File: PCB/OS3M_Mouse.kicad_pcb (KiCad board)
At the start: 4 copper layers, 60.8 x 61.3 mm, 47 parts, among them J1 DBG_HDR, J2 USB_C_Receptacle_USB2.0, J3 EXP_HDR, SW1 SW_Push, U1 AP2112K-3.3, U2 LDC1614, U3 STM32F042F6P6, U4 LDC1612, U5 USBLC6-2SC6, X1 ASV-40.000MHz

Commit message: Swapped inner layers to get GND plane close to components, fixed shorted UART
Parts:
- added TP1: TestPoint, TestPoint:TestPoint_Pad_D1.0mm, B.Cu at (149.5, 74.7)
- added TP2: TestPoint, TestPoint:TestPoint_Pad_D1.0mm, B.Cu at (141.8, 74.1)
- added TP3: TestPoint, TestPoint:TestPoint_Pad_D1.0mm, B.Cu at (143.6, 75.1)
- added TP4: TestPoint, TestPoint:TestPoint_Pad_D1.0mm, B.Cu at (141.8, 76.1)
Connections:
- U3 pad 10: unconnected-(U3-Pad10) -> Net-(U3-PA4)
- U3 pad 11: unconnected-(U3-Pad11) -> Net-(U3-PA5)
- U3 pad 12: unconnected-(U3-Pad12) -> Net-(U3-PA6)
- U3 pad 13: unconnected-(U3-Pad13) -> Net-(U3-PA7)
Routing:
- net Net-(U3-PA7): track 0.00 -> 2.40 mm, vias 0 -> 1
- net Net-(U3-PA4): track 0.00 -> 2.04 mm, vias 0 -> 1
- net Net-(U3-PA6): track 0.00 -> 1.95 mm, vias 0 -> 1
- net /UART2_TX: track 39.4 -> 40.6 mm
- net +3.3V: track 90.9 -> 89.8 mm
- net /UART2_RX: track 43.7 -> 44.4 mm, vias 2 -> 3
- net Net-(U3-PA5): track 0.00 -> 0.60 mm, vias 0 -> 1
- net /LDC1614_INTB: track 34.8 -> 34.2 mm
- added copper zone on In2.Cu, net +3.3V
- added copper zone on In1.Cu, net GND
- added copper zone on In2.Cu, net VBUS
- removed copper zone on In1.Cu, net +3.3V
- removed copper zone on In2.Cu, net GND
- removed copper zone on In1.Cu, net VBUS

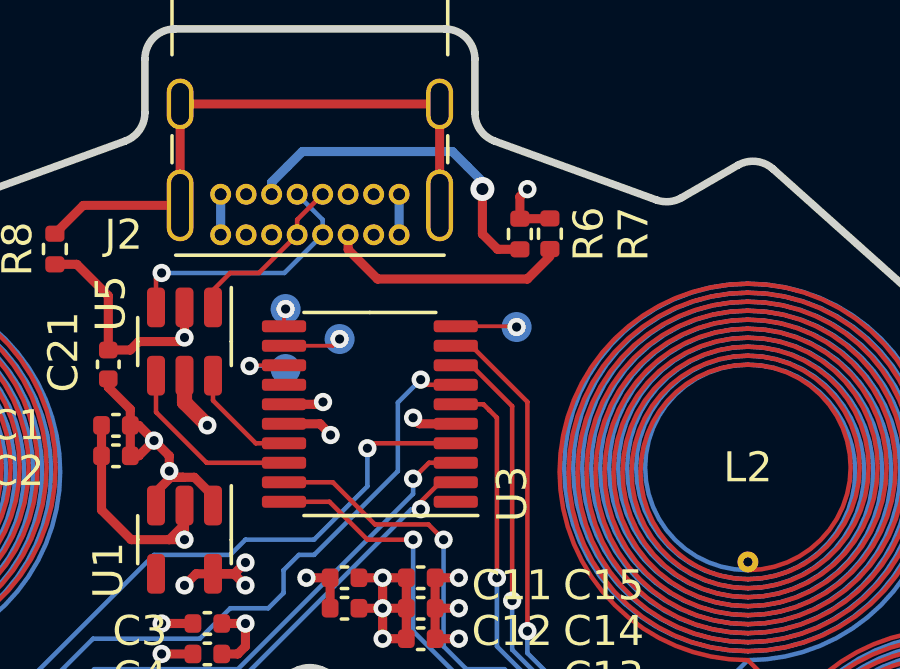
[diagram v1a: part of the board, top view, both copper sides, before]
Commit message: Moved test points
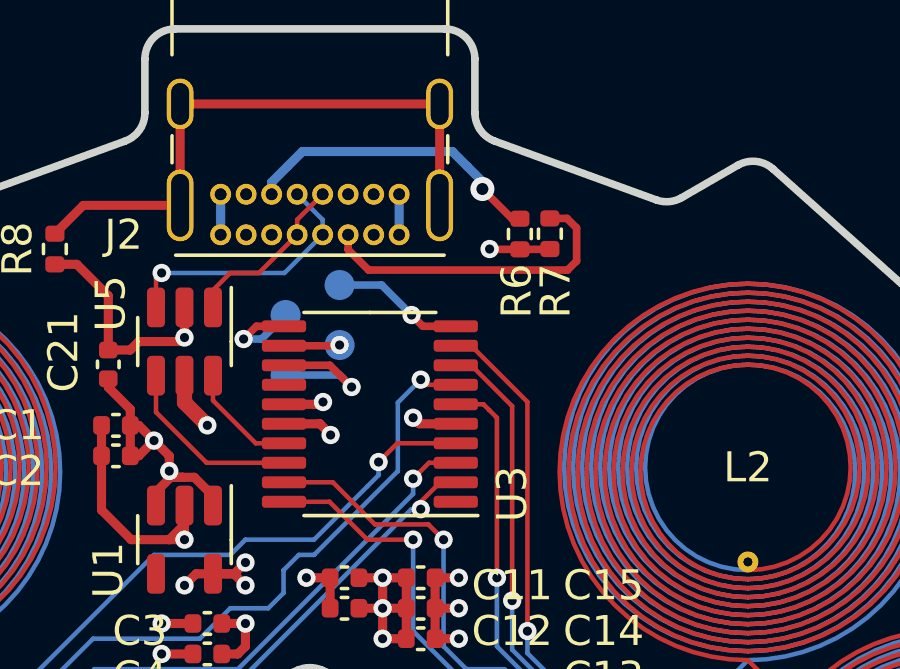
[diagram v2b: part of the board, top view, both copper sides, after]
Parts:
- moved TP1 6.06 mm to (143.6, 73.3)
- moved TP2 0.20 mm to (141.8, 74.3)
- moved TP3 0.20 mm to (143.6, 75.3)
- moved TP4 0.20 mm to (141.8, 76.3)
- turned R6 to -90 degrees
- turned R7 to -90 degrees
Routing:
- net /CC1: track 7.94 -> 10.7 mm
- net Net-(U3-PA7): track 2.40 -> 5.06 mm
- net Net-(U3-PA5): track 0.60 -> 3.25 mm
- net Net-(U3-PA4): track 2.04 -> 4.44 mm
- net /CC2: track 11.5 -> 10.2 mm
